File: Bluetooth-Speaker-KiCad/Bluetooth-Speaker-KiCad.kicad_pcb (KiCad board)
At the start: 4 copper layers, 32 parts, among them J1 USB4105-GF-A, J2 Screw_Terminal_01x02, J3 Screw_Terminal_01x02, Q1 Q_PMOS_DSG, U1 TPD4E02B04DQA, U2 MAX1811, U3 RT6150B-33GQW, U4 MAX98357A, U5 ESP32-C3-WROOM-02

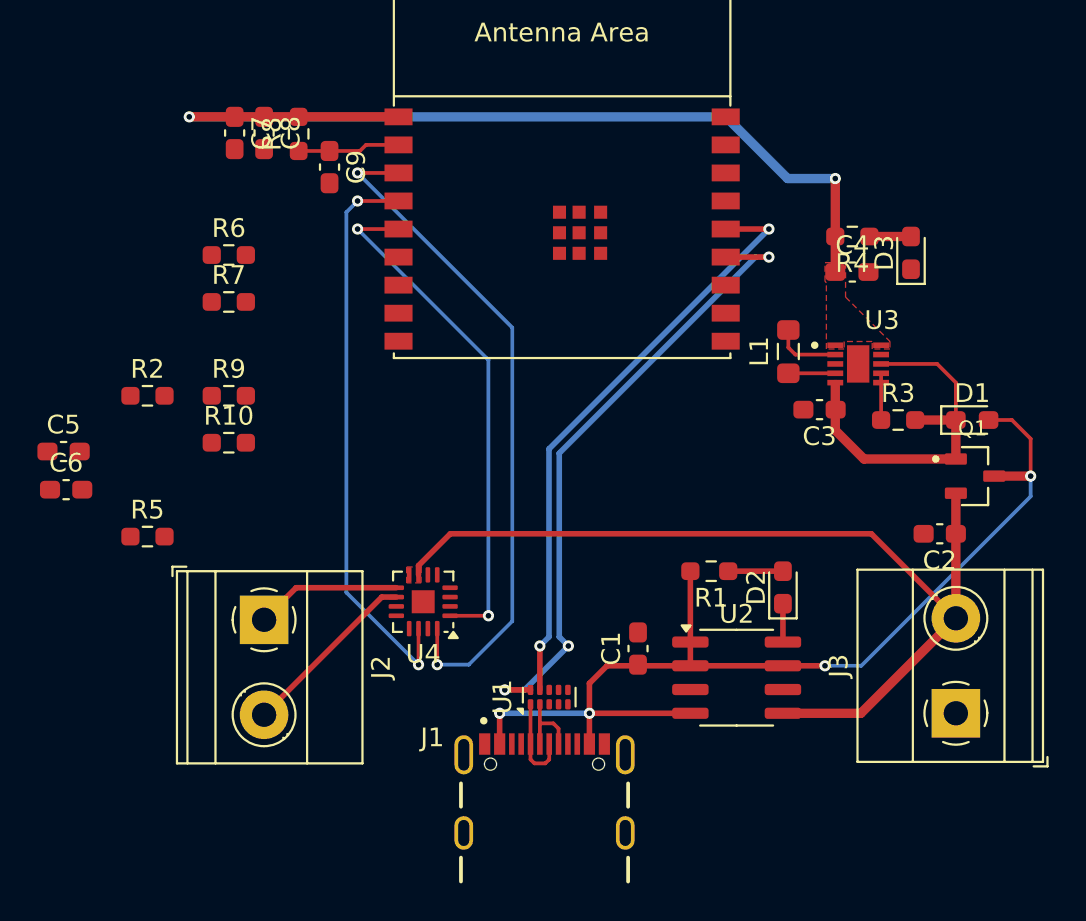
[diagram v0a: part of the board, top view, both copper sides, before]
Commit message: Updated layout
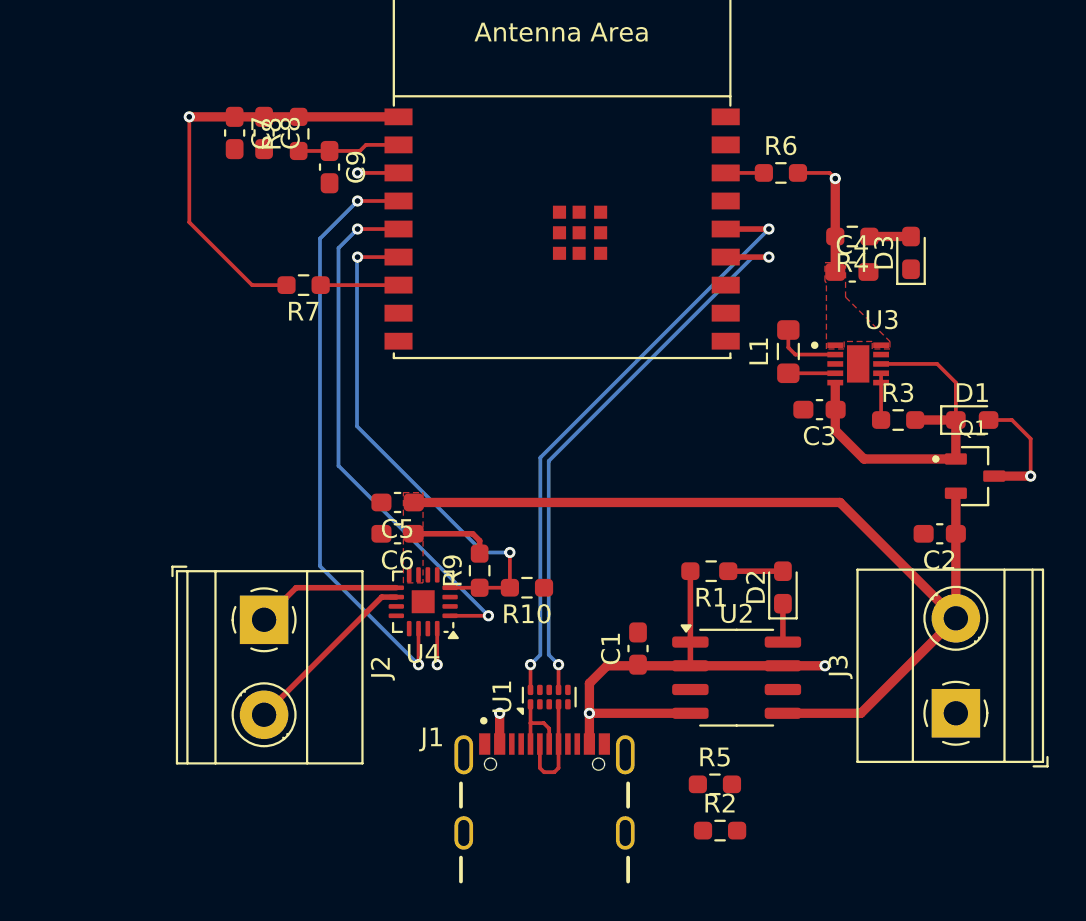
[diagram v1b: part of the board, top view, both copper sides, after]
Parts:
- moved R2 38.5 mm to (154.4, 134.9)
- moved R5 33.1 mm to (154.1, 132.4)
- moved R6 29.9 mm to (157.6, 99.7)
- moved C5 18.1 mm to (137.1, 117.3), turned to 180 degrees
- moved C6 17.9 mm to (137.1, 119.0), turned to 180 degrees
- moved R10 17.7 mm to (144.1, 121.9), turned to 180 degrees
- moved R9 16.4 mm to (141.5, 121.0), turned to 90 degrees
- moved R7 4.10 mm to (132.1, 105.7), turned to 180 degrees
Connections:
- R9 pad 2: +3.3V -> Battery_POS
- U1 pad 2: /D+ -> unconnected-(U1-IO2-Pad2)
- U1 pad 4: unconnected-(U1-IO3-Pad4) -> /D+
- U1 pad 7: unconnected-(U1-NC-Pad7) -> /DProtect_+
- U1 pad 9: /DProtect_+ -> unconnected-(U1-NC-Pad9)
- U5 pad 13: /DProtect_- -> /DProtect_+
- U5 pad 14: /DProtect_+ -> /DProtect_-
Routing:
- net /SD_MODE: track 0.00 -> 27.3 mm, vias 0 -> 2
- net +3.3V: track 52.1 -> 66.5 mm
- net /Boot_Strap_8: track 0.00 -> 4.16 mm
- net Battery_POS: track 49.9 -> 54.0 mm
- net +5V_USB: track 55.6 -> 59.1 mm
- net /Boot_Strap_2: track 0.00 -> 2.04 mm
- net /DProtect_-: track 34.1 -> 32.2 mm, vias 3 -> 2
- net /D+: track 4.07 -> 5.87 mm
- net /I2S_LRCLK: track 30.8 -> 31.9 mm
- net /DProtect_+: track 32.0 -> 31.1 mm
- net /I2S_BCLK: track 36.5 -> 37.5 mm
- net /D-: track 4.95 -> 4.07 mm
- net /I2S_DIN: track 27.8 -> 28.7 mm

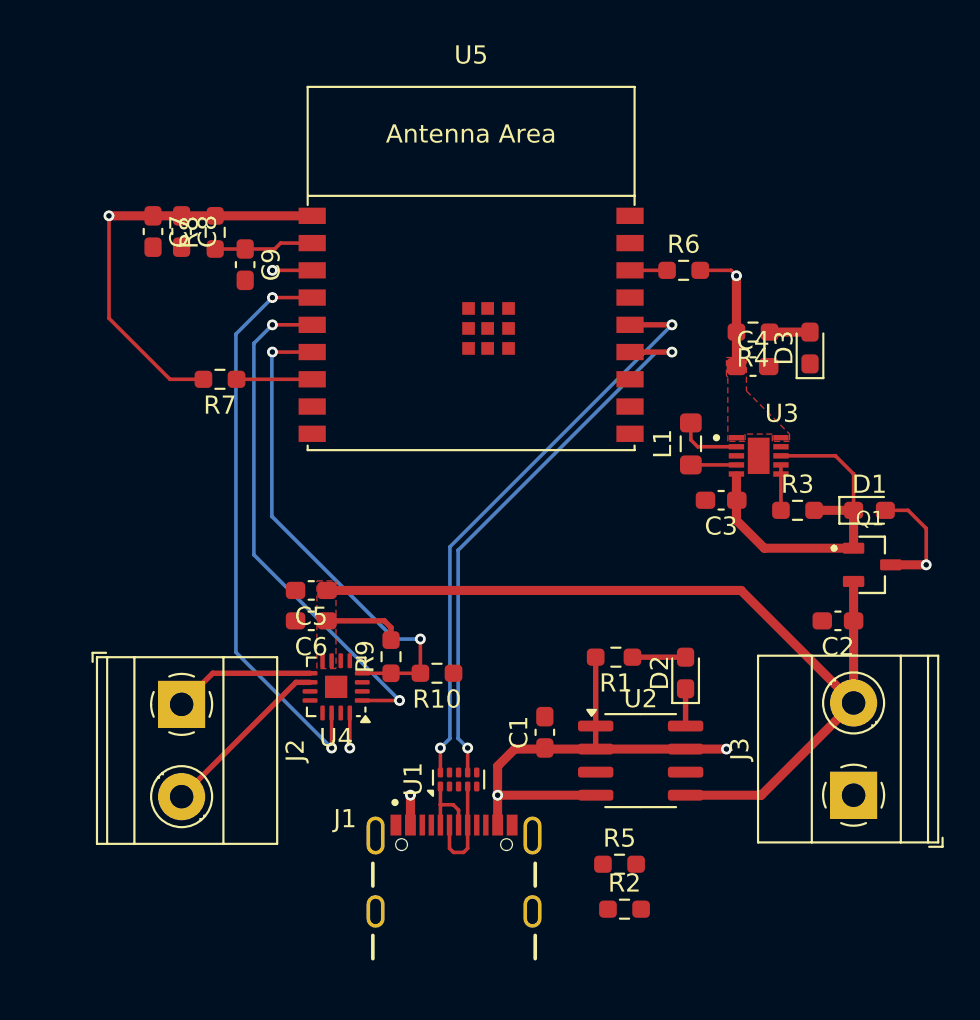
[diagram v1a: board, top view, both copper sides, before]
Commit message: Updated layout
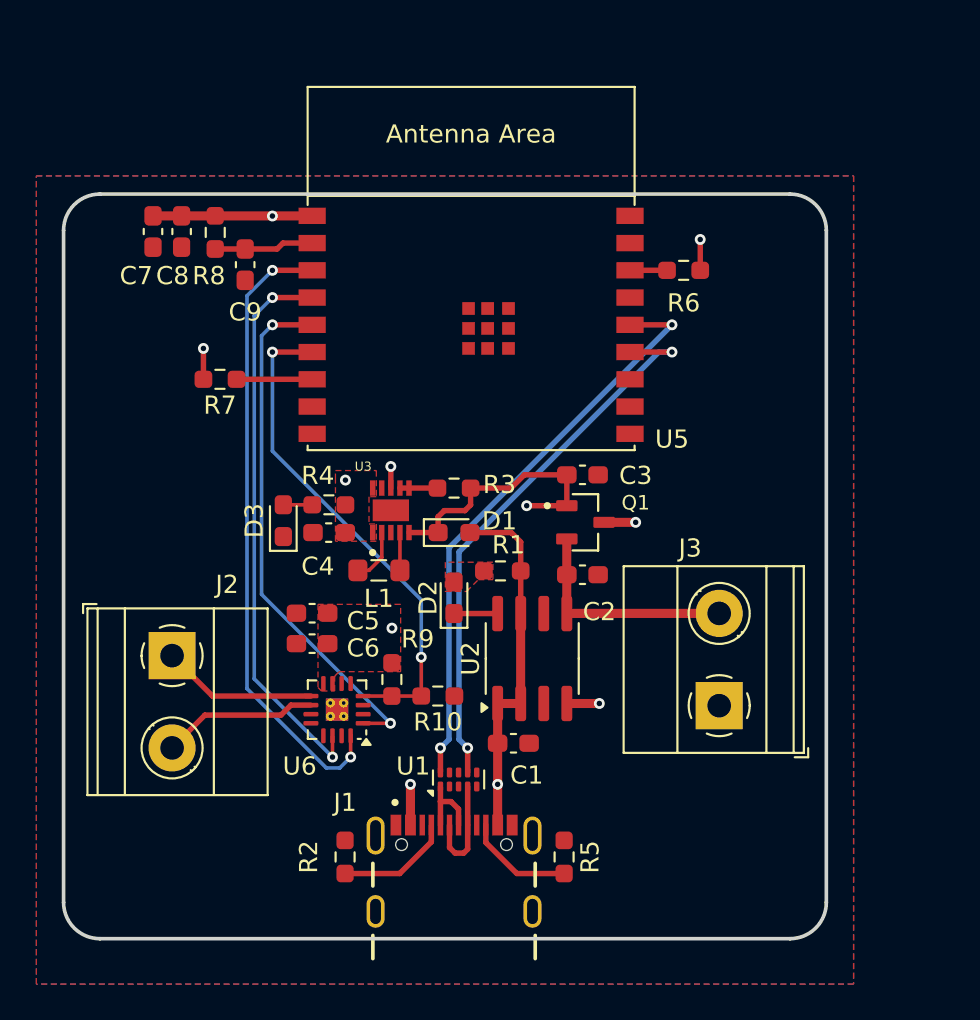
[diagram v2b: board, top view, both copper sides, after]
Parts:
- removed U4: MAX98357A, Package_DFN_QFN:TQFN-16-1EP_3x3mm_P0.5mm_EP1.23x1.23mm
- added U6: MAX98357A, Package_DFN_QFN:TQFN-16-1EP_3x3mm_P0.5mm_EP1.23x1.23mm_ThermalVias, F.Cu at (138.6, 123.9)
- moved D3 30.5 mm to (135.6, 113.5)
- moved R4 25.2 mm to (138.1, 112.6), turned to 0 degrees
- moved C4 25.1 mm to (138.1, 114.1), turned to 180 degrees
- moved D1 22.9 mm to (145.0, 114.1)
- moved U3 20.5 mm to (141.5, 112.9), turned to 90 degrees
- moved R3 19.0 mm to (145.0, 111.7)
- moved L1 18.5 mm to (140.9, 116.2), turned to 180 degrees
- moved Q1 16.0 mm to (152.2, 113.6)
- moved R2 15.7 mm to (139.0, 132.0), turned to -90 degrees
- moved C2 14.3 mm to (152.1, 116.5), turned to 0 degrees
- moved D2 13.4 mm to (145.0, 117.7)
- moved J3 8.89 mm to (159.6, 123.7)
- moved U2 8.20 mm to (149.3, 121.1), turned to 90 degrees
- moved R1 7.93 mm to (147.6, 116.2), turned to 0 degrees
- moved C3 7.76 mm to (152.1, 111.0), turned to 0 degrees
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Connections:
- J3 pad 1: /Battery_NEG -> GND
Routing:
- net Battery_POS: track 54.0 -> 30.9 mm, vias 0 -> 1
- net +5V_USB: track 59.1 -> 50.1 mm
- net Net-(J1-CC1): track 0.00 -> 6.40 mm
- net Net-(J1-CC2): track 0.00 -> 5.98 mm
- net +3.3V: track 66.5 -> 61.3 mm, vias 2 -> 4
- net Net-(D1-K): track 20.2 -> 24.5 mm, vias 0 -> 2
- net Net-(D2-A): track 2.93 -> 0.00 mm
- net /I2S_BCLK: track 37.5 -> 34.7 mm
- net /I2S_LRCLK: track 31.9 -> 30.9 mm
- net /Speaker_NEG: track 9.68 -> 8.62 mm
- net /Speaker_POS: track 7.78 -> 8.57 mm
- net Net-(D3-A): track 2.22 -> 1.59 mm
- net Net-(U3-LX2): track 3.61 -> 2.98 mm
- added copper zone on B.Cu, net GND
- added copper zone on F.Cu, net GND
- added copper zone on In1.Cu, net GND
- added copper zone on In2.Cu, net GND
- added copper zone on F.Cu, net Net-(D2-A)
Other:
- board outline added: 42 x 41 mm

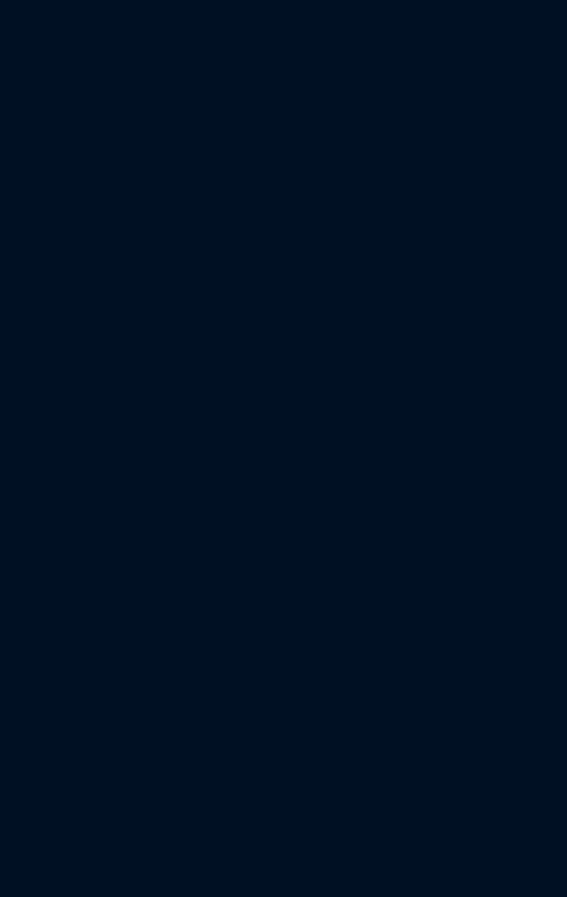
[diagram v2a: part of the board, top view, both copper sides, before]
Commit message: Removed mounting holes
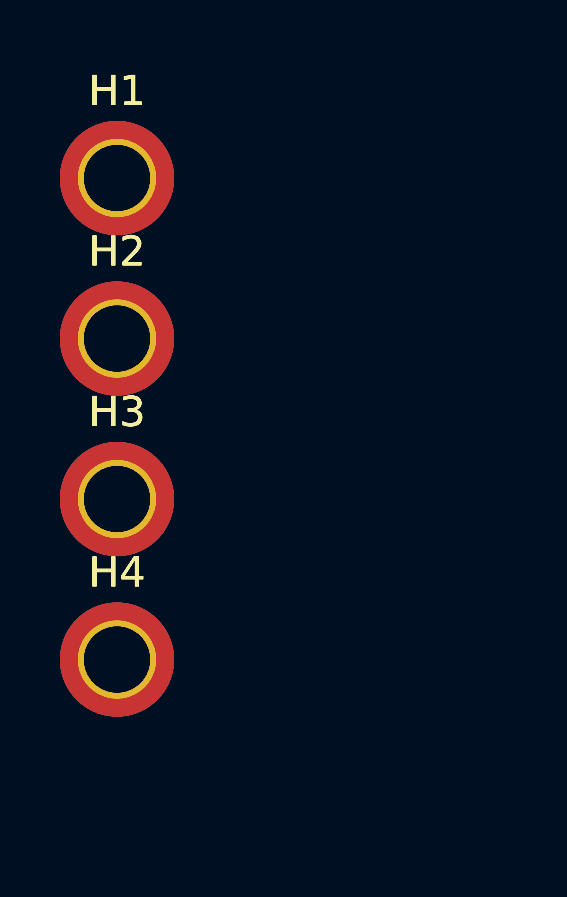
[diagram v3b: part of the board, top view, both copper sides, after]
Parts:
- added H1: MountingHole_Pad_MP, MountingHole:MountingHole_2.2mm_M2_ISO14580_Pad_TopBottom, F.Cu at (2.17, 2.17)
- added H1: MountingHole_Pad, MountingHole:MountingHole_2.2mm_M2_DIN965_Pad_TopBottom, F.Cu at (2.17, 2.17)
- added H2: MountingHole_Pad, MountingHole:MountingHole_2.2mm_M2_DIN965_Pad_TopBottom, F.Cu at (2.17, 7.53)
- added H2: MountingHole_Pad_MP, MountingHole:MountingHole_2.2mm_M2_ISO14580_Pad_TopBottom, F.Cu at (2.17, 7.53)
- added H3: MountingHole_Pad, MountingHole:MountingHole_2.2mm_M2_DIN965_Pad_TopBottom, F.Cu at (2.17, 12.9)
- added H3: MountingHole_Pad_MP, MountingHole:MountingHole_2.2mm_M2_ISO14580_Pad_TopBottom, F.Cu at (2.17, 12.9)
- added H4: MountingHole_Pad, MountingHole:MountingHole_2.2mm_M2_DIN965_Pad_TopBottom, F.Cu at (2.17, 18.2)
- added H4: MountingHole_Pad_MP, MountingHole:MountingHole_2.2mm_M2_ISO14580_Pad_TopBottom, F.Cu at (2.17, 18.2)

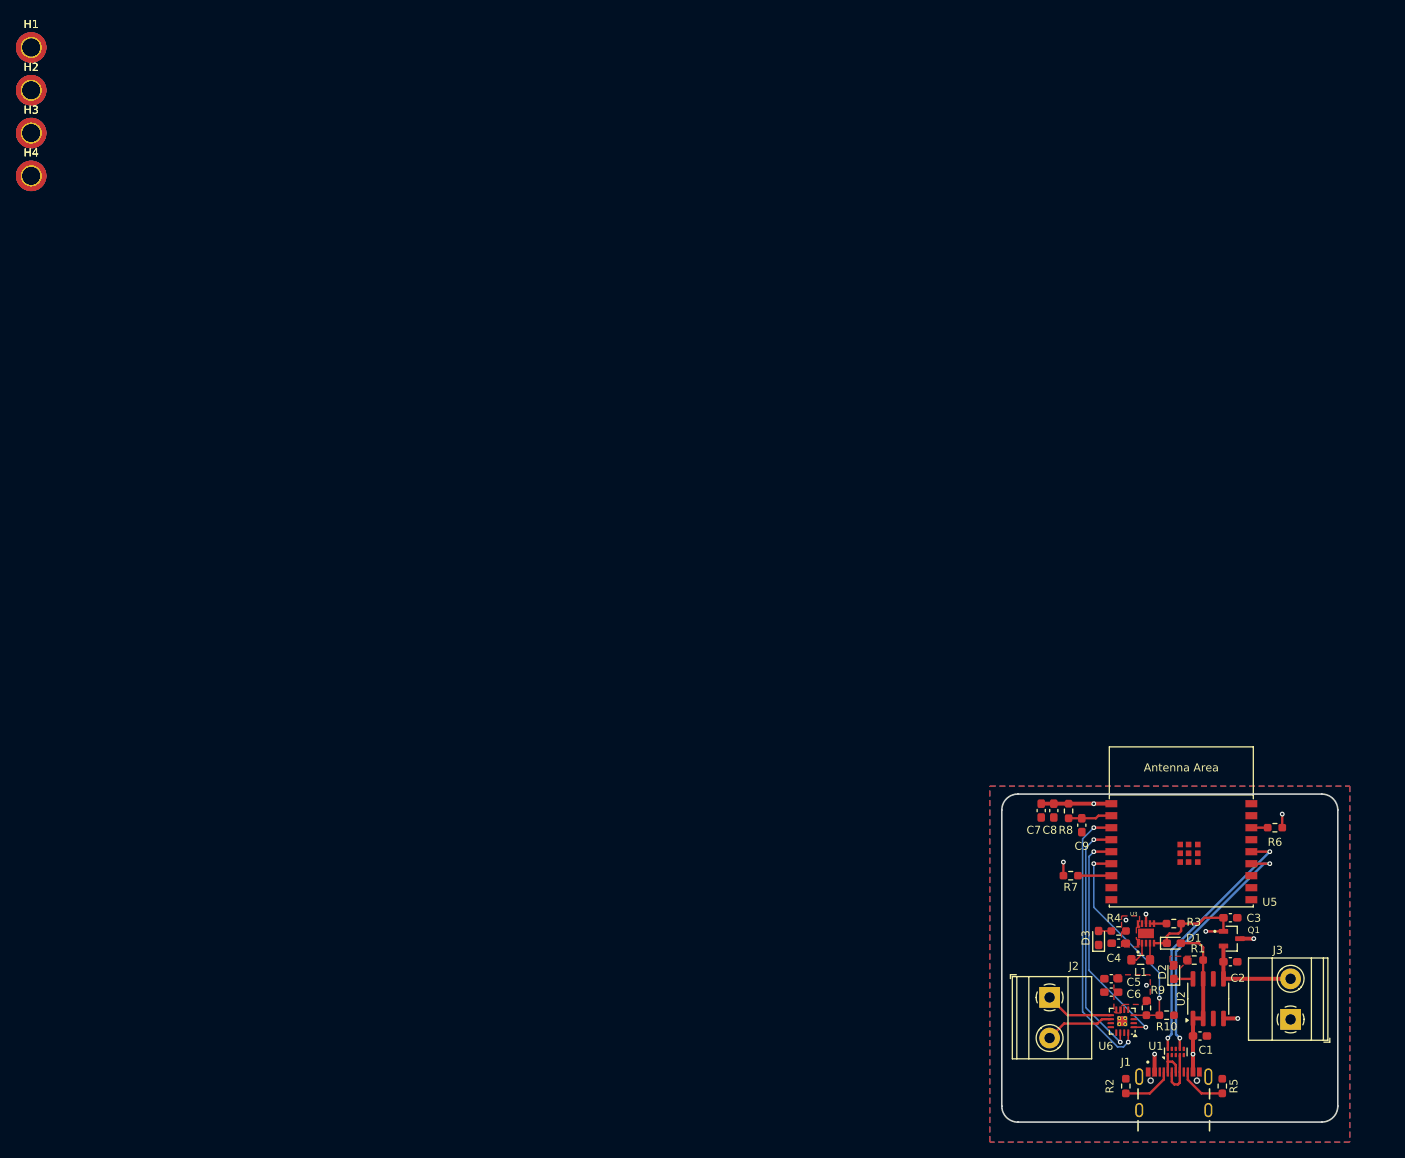
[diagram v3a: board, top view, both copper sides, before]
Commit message: Updated layout with switches
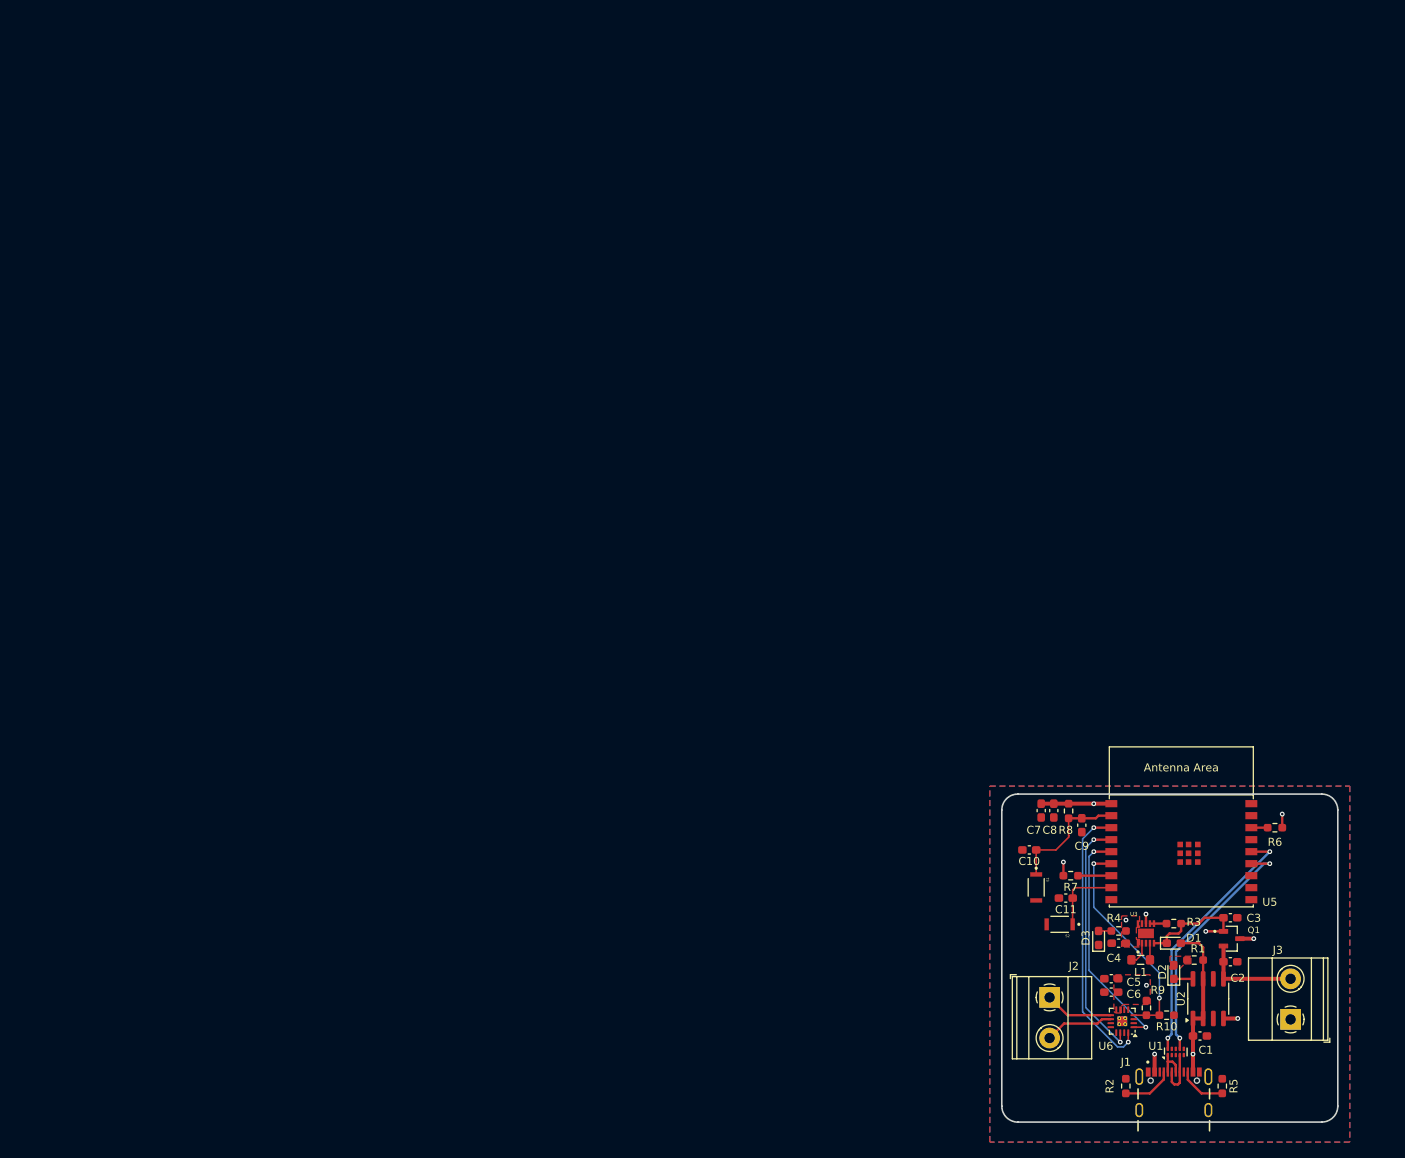
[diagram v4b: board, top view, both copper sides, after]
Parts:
- removed H1, H2, H3, H4: MountingHole_Pad_MP, MountingHole:MountingHole_2.2mm_M2_ISO14580_Pad_TopBottom
- removed H1, H2, H3, H4: MountingHole_Pad, MountingHole:MountingHole_2.2mm_M2_DIN965_Pad_TopBottom
- added C10: 0.1u, Capacitor_SMD:C_0603_1608Metric_Pad1.08x0.95mm_HandSolder, F.Cu at (126.9, 102.5)
- added C11: 0.1u, Capacitor_SMD:C_0603_1608Metric_Pad1.08x0.95mm_HandSolder, F.Cu at (131.5, 108.5)
- added S1: EVP-AWCD4A, EVP_AWCD4A (1):SW_EVP-AWCD4A, F.Cu at (127.8, 107.2)
- added S2: EVP-AWCD4A, EVP_AWCD4A (1):SW_EVP-AWCD4A, F.Cu at (130.7, 111.8)
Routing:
- net /ESP_EN: track 5.47 -> 15.6 mm
- net /Boot_Strap_9: track 0.00 -> 9.25 mm
